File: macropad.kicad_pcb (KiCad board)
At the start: 2 copper layers, 103.2 x 57.1 mm, 32 parts, among them SW1 Rotary_Encoder_Switch, SW2 SW_Push, U1 ProMicro

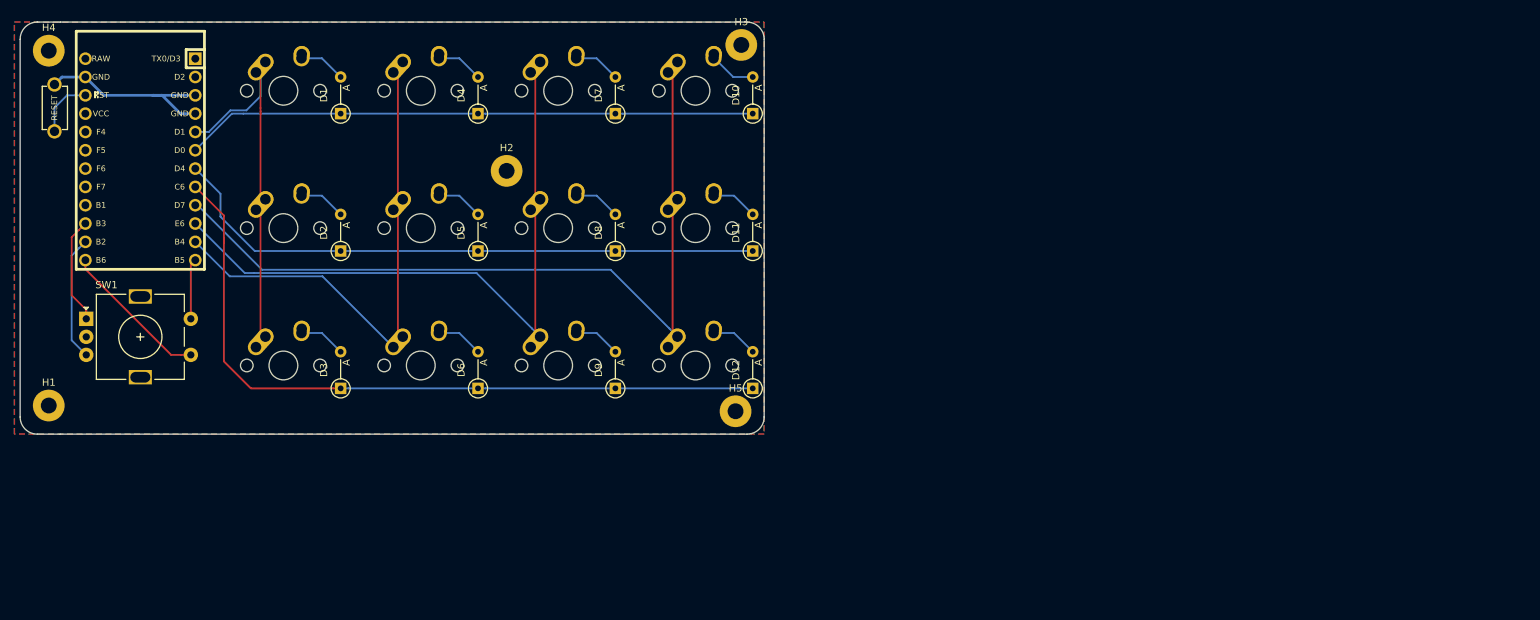
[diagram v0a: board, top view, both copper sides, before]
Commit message: pcb overhaul
Added second rotary encoder
Moved Pro Micro under switches
Made backplate
Added artwork
Made pcb smaller overall
Added mousebites as symbol
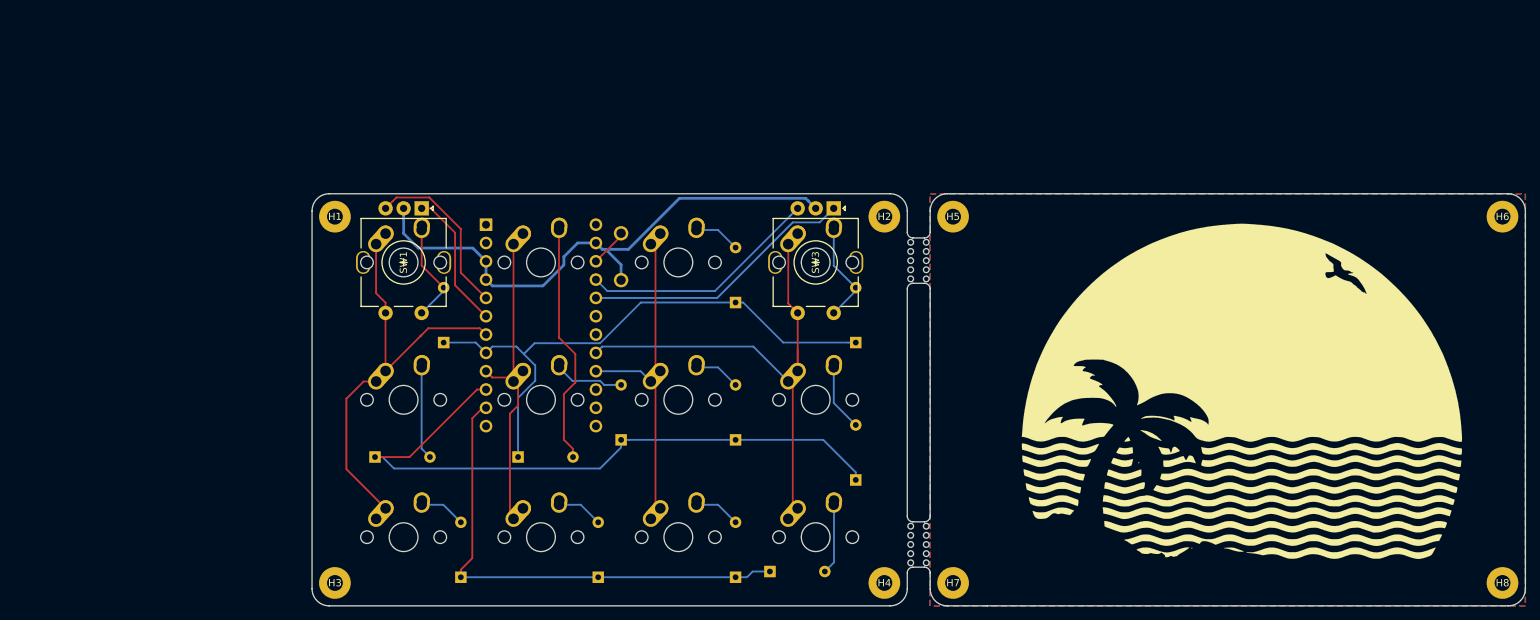
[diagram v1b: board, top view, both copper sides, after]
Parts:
- added B1: mousebites, random-keyboard-parts:breakaway-mousebites, F.Cu at (188.8, 63.2)
- added B2: mousebites, random-keyboard-parts:breakaway-mousebites, F.Cu at (190.5, 63.2)
- added B3: mousebites, random-keyboard-parts:breakaway-mousebites, F.Cu at (190.5, 102.6)
- added B4: mousebites, random-keyboard-parts:breakaway-mousebites, F.Cu at (188.8, 102.6)
- added G***: LOGO, macropad:wef, F.Cu at (232.6, 84.1)
- added H6: MountingHole, MountingHole:MountingHole_2.2mm_M2_Pad, F.Cu at (270.7, 57.1)
- added H7: MountingHole, MountingHole:MountingHole_2.2mm_M2_Pad, F.Cu at (194.5, 108.0)
- added H8: MountingHole, MountingHole:MountingHole_2.2mm_M2_Pad, F.Cu at (270.7, 108.0)
- added SW3: Ec11, macropad:RotaryEncoder_Alps_EC11E-Switch_Vertical_H20mm, F.Cu at (175.4, 63.5)
- D1, D10, D11, D12, D2, D3, D4, D5, D6, D7, D8, D9: value D_Small -> 1N4148; footprint Diode_THT:D_DO-35_SOD27_P5.08mm_Vertical_AnodeUp -> Diode_THT:D_DO-35_SOD27_P7.62mm_Horizontal; moved to B.Cu
- SW1: value Rotary_Encoder_Switch -> Ec11
- U1: moved to F.Cu
- moved H4 137.4 mm to (184.9, 108.0)
- moved H3 93.5 mm to (108.7, 108.0)
- moved SW2 81.2 mm to (148.4, 62.7), turned to 90 degrees
- moved U1 60.1 mm to (137.3, 72.2)
- moved H2 52.8 mm to (184.9, 57.1)
- moved D4 47.9 mm to (134.1, 90.5), turned to 0 degrees
- moved H1 47.6 mm to (108.7, 57.1)
- moved H5 40.5 mm to (194.5, 57.1)
- moved SW1 37.9 mm to (118.3, 63.5), turned to 270 degrees
- moved D1 34.8 mm to (123.8, 74.6)
- moved D10 34.8 mm to (181.0, 74.6)
- moved D11 34.8 mm to (181.0, 93.7)
- moved D5 32.9 mm to (148.4, 88.1)
- moved D7 31.0 mm to (164.3, 69.1)
- moved D8 31.0 mm to (164.3, 88.1)
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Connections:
- net RESET renamed Net-(SW2-Pad2)
- SW1 pad S1: SW25A -> COL0
- SW1 pad S2: SW25B -> Net-(D1-Pad2)
- U1 pad 10: COL2 -> ROW1
- U1 pad 11: COL1 -> ROW2
- U1 pad 12: SW25B -> Net-(U1-Pad12)
- U1 pad 13: SW25A -> Net-(U1-Pad13)
- U1 pad 14: ENCB -> Net-(U1-Pad14)
- U1 pad 15: ENCA -> Net-(U1-Pad15)
- U1 pad 16: Net-(U1-Pad16) -> COL2
- U1 pad 17: Net-(U1-Pad17) -> COL3
- U1 pad 20: Net-(U1-Pad20) -> ENCA1
- U1 pad 21: VCC -> ENCB1
- U1 pad 5: COL0 -> ENCB
- U1 pad 6: ROW0 -> ENCA
- U1 pad 7: ROW1 -> COL0
- U1 pad 8: ROW2 -> ROW0
- U1 pad 9: COL3 -> COL1
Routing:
- net GND: track 27.9 -> 78.2 mm
- net COL2: track 94.9 -> 47.4 mm
- net COL3: track 113.7 -> 71.8 mm
- net ENCA1: track 0.00 -> 38.1 mm
- net ENCB1: track 0.00 -> 33.4 mm
- net ROW2: track 101.4 -> 68.6 mm
- net COL1: track 73.4 -> 43.4 mm
- net Net-(D4-Pad2): track 6.51 -> 33.6 mm
- net SW25A: track 20.8 -> 0.00 mm
- net SW25B: track 8.39 -> 0.00 mm
- net ROW1: track 83.9 -> 91.8 mm
- net Net-(D10-Pad2): track 6.51 -> 14.0 mm
- net Net-(D1-Pad2): track 6.51 -> 14.0 mm
- net COL0: track 55.4 -> 61.9 mm
- net Net-(D2-Pad2): track 6.51 -> 12.9 mm
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- added copper zone on B.Cu, net (none)
- added copper zone on F.Cu, net (none)
- removed copper zone on B.Cu, net GND
- removed copper zone on F.Cu, net GND
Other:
- board size 103.2 x 57.1 mm -> 168.3 x 57.2 mm

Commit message: Small fixes to PCB
Rotated rotary encoders 180*
Changed switch footprint to MX_Only
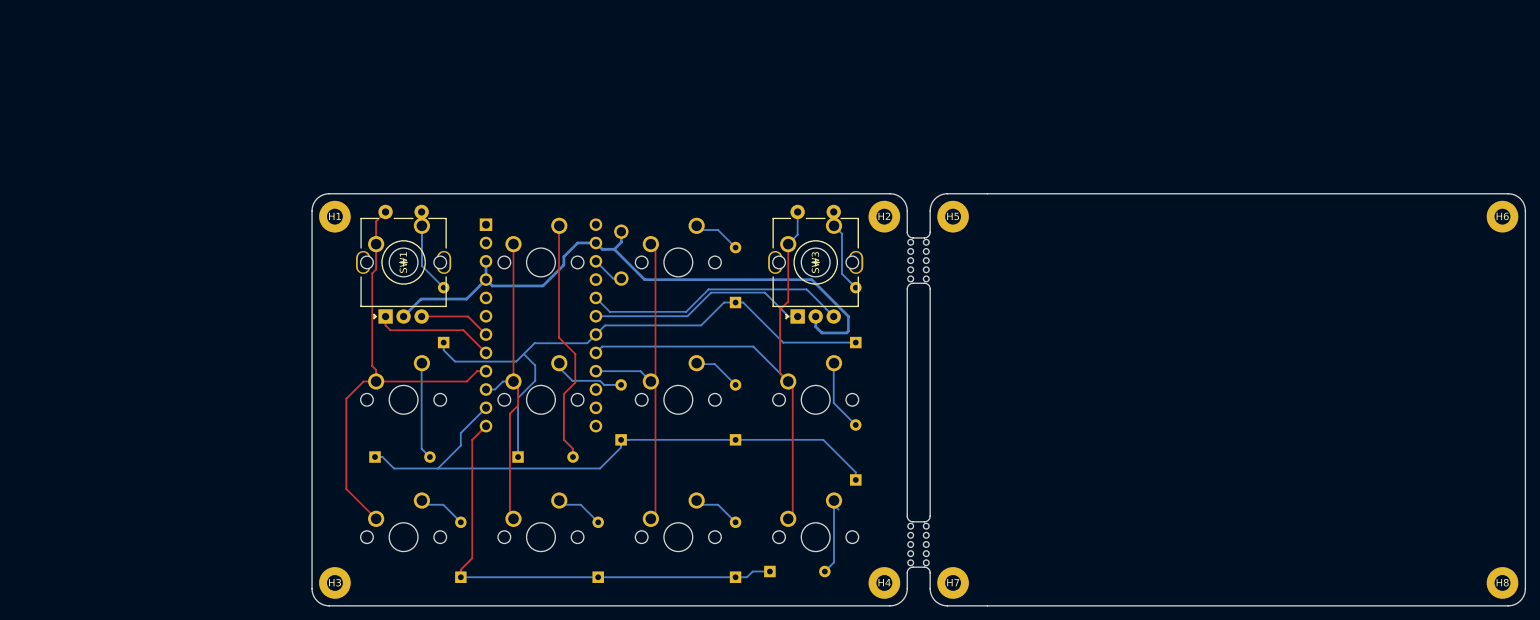
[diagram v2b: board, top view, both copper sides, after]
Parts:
- removed G***: LOGO, macropad:wef
- MX1, MX10, MX11, MX12, MX2, MX3, MX4, MX5, MX6, MX7, MX8, MX9: footprint MX_Alps_Hybrid:MX-1U-NoLED -> MX_Only:MXOnly-1U-NoLED
- moved SW2 0.22 mm to (148.5, 62.5), turned to 270 degrees
- turned SW1 to 90 degrees
- turned SW3 to 90 degrees
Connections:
- SW1 pad S1: COL0 -> Net-(D1-Pad2)
- SW1 pad S2: Net-(D1-Pad2) -> COL0
- SW3 pad S1: COL3 -> Net-(D10-Pad2)
- SW3 pad S2: Net-(D10-Pad2) -> COL3
- U1 pad 10: ROW1 -> COL1
- U1 pad 11: ROW2 -> ROW1
- U1 pad 12: Net-(U1-Pad12) -> ROW2
- U1 pad 18: Net-(U1-Pad18) -> ROW0
- U1 pad 19: Net-(U1-Pad19) -> ENCA1
- U1 pad 20: ENCA1 -> ENCB1
- U1 pad 21: ENCB1 -> VCC
- U1 pad 5: ENCB -> Net-(U1-Pad5)
- U1 pad 6: ENCA -> Net-(U1-Pad6)
- U1 pad 7: COL0 -> ENCB
- U1 pad 8: ROW0 -> ENCA
- U1 pad 9: COL1 -> COL0
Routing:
- net ENCB: track 23.9 -> 9.97 mm
- net ROW1: track 91.8 -> 83.7 mm
- net ENCA1: track 38.1 -> 30.7 mm
- net GND: track 78.2 -> 85.4 mm
- net ENCB1: track 33.4 -> 36.6 mm
- net ROW2: track 68.6 -> 65.6 mm
- net ENCA: track 19.4 -> 16.8 mm
- net Net-(D1-Pad2): track 14.0 -> 11.8 mm
- net Net-(D10-Pad2): track 14.0 -> 11.8 mm
- net COL0: track 61.9 -> 63.8 mm
- net COL3: track 71.8 -> 73.6 mm
- net Net-(SW2-Pad2): track 5.33 -> 4.52 mm
- net ROW0: track 79.7 -> 80.5 mm
- removed copper zone on B.Cu, net (none)
- removed copper zone on F.Cu, net (none)

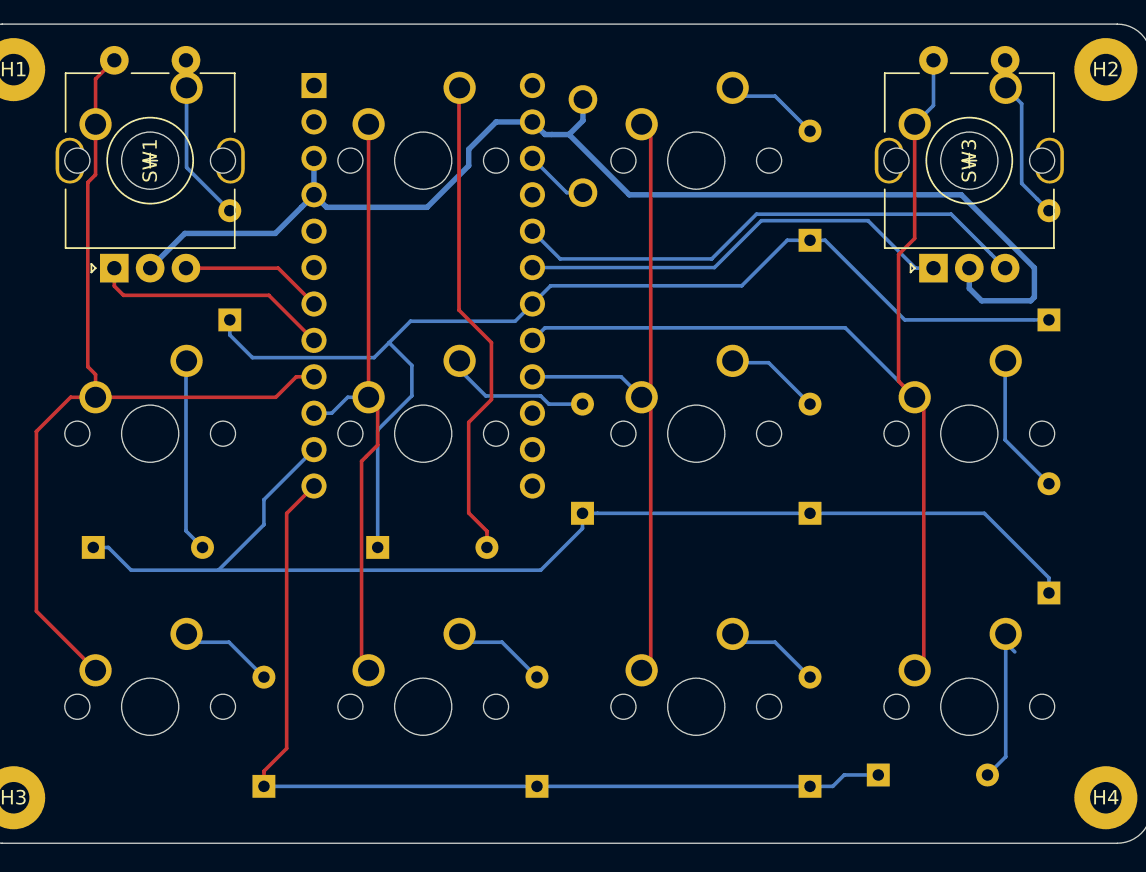
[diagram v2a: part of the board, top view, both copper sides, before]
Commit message: Small placement adjustments
Added credit
Made diode placement more consistent
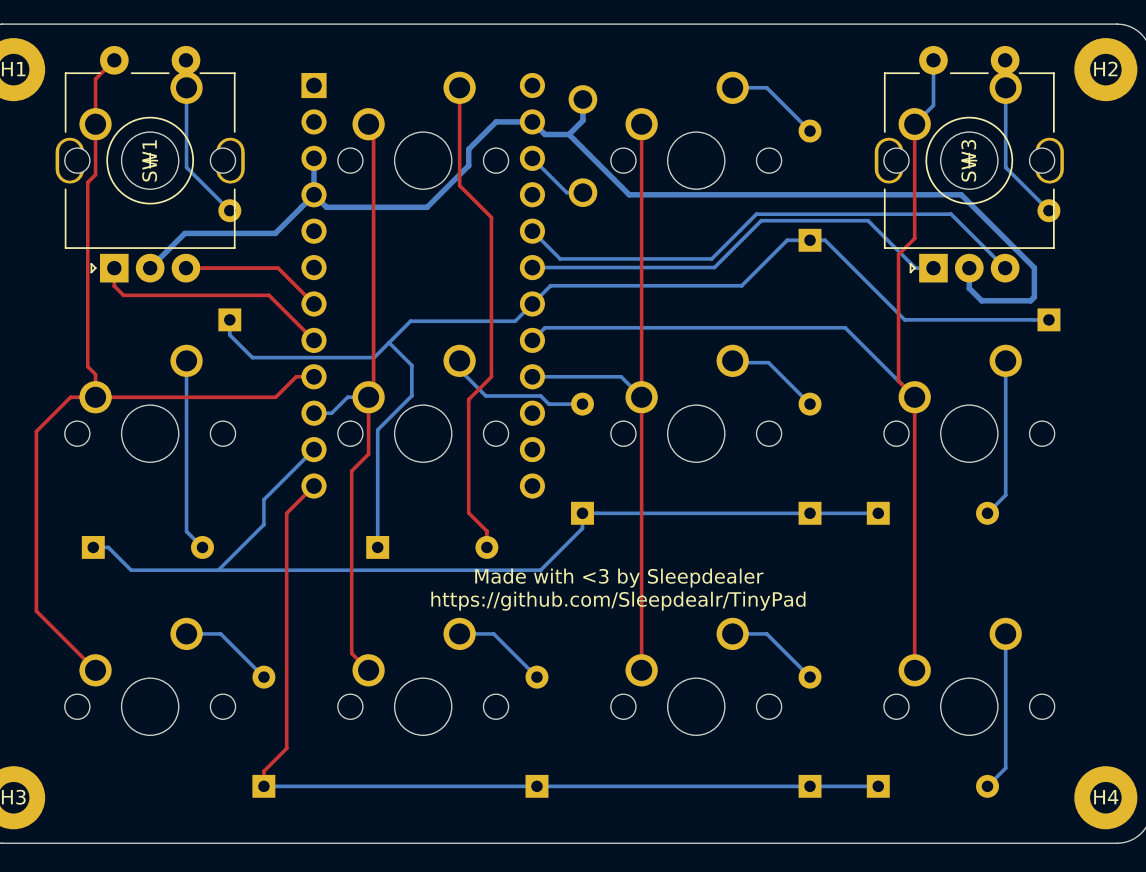
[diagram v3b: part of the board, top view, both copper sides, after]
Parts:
- moved D11 13.1 mm to (169.1, 88.1), turned to 0 degrees
- moved D12 0.79 mm to (169.1, 107.2)
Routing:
- net ROW1: track 83.7 -> 68.9 mm
- net Net-(D11-Pad2): track 9.26 -> 11.6 mm
- net COL3: track 73.6 -> 75.0 mm
- net COL1: track 43.3 -> 44.5 mm
- net COL2: track 47.4 -> 48.1 mm
- net Net-(D4-Pad2): track 33.6 -> 34.2 mm
- net Net-(D2-Pad2): track 12.9 -> 13.5 mm
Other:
- board text added: "Made with <3 by Sleepdealer https://github.com/Sleepdealr/TinyPad"

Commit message: Changed diode placement
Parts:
- SW2: footprint macropad:TACT_SWITCH_TVBP06 -> random-keyboard-parts:Jumper-UserFriendly-Small
- moved D3 17.9 mm to (108.7, 103.2)
- moved D12 16.4 mm to (184.9, 103.2), turned to 90 degrees
- moved D1 16.1 mm to (108.7, 69.1)
- moved D8 11.1 mm to (154.0, 92.1), turned to 0 degrees
- moved SW2 7.00 mm to (148.8, 55.5)
- moved D10 6.20 mm to (184.9, 69.8)
- moved D11 5.61 mm to (173.0, 92.1)
- moved D2 1.77 mm to (113.5, 92.1)
- moved D6 1.77 mm to (146.8, 106.4)
- moved D9 1.77 mm to (165.9, 106.4)
- moved D4 1.59 mm to (134.1, 92.1)
- moved D7 1.59 mm to (165.9, 69.1)
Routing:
- net ROW2: track 65.3 -> 138.1 mm
- net ROW0: track 80.5 -> 105.0 mm
- net ROW1: track 68.9 -> 77.9 mm
- net Net-(D8-Pad2): track 6.82 -> 15.6 mm
- net Net-(SW2-Pad2): track 4.52 -> 11.9 mm
- net GND: track 85.4 -> 91.4 mm
- net Net-(D3-Pad2): track 6.65 -> 12.5 mm
- net Net-(D12-Pad2): track 11.2 -> 7.38 mm
- net Net-(D11-Pad2): track 11.6 -> 15.4 mm
- net Net-(D1-Pad2): track 11.8 -> 15.3 mm
- net Net-(D7-Pad2): track 6.65 -> 8.23 mm
- net Net-(D4-Pad2): track 34.2 -> 35.8 mm
- net ENCB1: track 36.6 -> 35.3 mm
- net Net-(D10-Pad2): track 11.8 -> 10.5 mm
- net Net-(D9-Pad2): track 6.65 -> 7.91 mm
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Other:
- board text added: "Made by Sleepdealer"
- board text removed: "Made with <3 by Sleepdealer https://github.com/Sleepdealr/TinyPad"
